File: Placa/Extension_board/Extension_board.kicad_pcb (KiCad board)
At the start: 2 copper layers, 61 x 20.3 mm, 12 parts, among them J1 Conn_01x05_Male, J2 USB_B_Micro, J3 Conn_01x04_Male, U1 STEVAL-STLCS01V1

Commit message: Version 2.1 del proyecto
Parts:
- removed D3: LED, Diode_SMD:D_0805_2012Metric
- removed R2, R3: 1Ω, Resistor_SMD:R_0805_2012Metric
- removed R5: 1kΩ, Resistor_SMD:R_0805_2012Metric
- J1: value Conn_01x05_Male -> USB_B_Micro; footprint Connector_PinHeader_1.27mm:PinHeader_1x05_P1.27mm_Vertical -> Connector_USB:USB_Micro-B_Wuerth_629105150521
- J3: footprint Connector_PinHeader_1.27mm:PinHeader_1x04_P1.27mm_Vertical -> Connector_PinHeader_1.00mm:PinHeader_1x04_P1.00mm_Vertical_SMD_Pin1Left
- R1: value 1Ω -> 1,2Ω
- moved J2 64.4 mm to (102.9, 64.8), turned to 270 degrees
- moved R1 46.6 mm to (111.8, 55.5), turned to 270 degrees
- moved R4 41.6 mm to (108.0, 55.9), turned to 270 degrees
- moved D2 35.6 mm to (108.0, 52.1), turned to 270 degrees
- moved D1 32.1 mm to (111.6, 52.1), turned to 90 degrees
- moved J3 17.0 mm to (121.9, 66.0), turned to 90 degrees
- moved J1 12.2 mm to (102.6, 49.3), turned to 270 degrees
- moved U1 11.5 mm to (121.7, 56.6), turned to 0 degrees
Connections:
- J1 pad 1: Net-(J1-Pad1) -> /SWDIO
- J1 pad 3: /GND -> /RESET
- J1 pad 4: /SWDIO -> Net-(J1-Pad4)
- J1 pad 5: /RESET -> /GND
- J3 pad 1: /V_USB -> /VIN
- R1 pad 1: Net-(R1-Pad1) -> /VIN
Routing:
- net /RXD-USB_DM: track 63.4 -> 12.2 mm, vias 2 -> 0
- net /V_USB: track 62.4 -> 11.9 mm
- net /RXD-USB_DP: track 51.4 -> 12.5 mm
- net /SWDCLK: track 64.1 -> 26.9 mm, vias 2 -> 0
- net /GND: track 104.8 -> 97.9 mm, vias 2 -> 0
- net /I2C_SDA: track 14.6 -> 10.5 mm
- net Net-(D3-Pad2): track 3.55 -> 0.00 mm
- net /SWDIO: track 23.9 -> 26.7 mm
- net Net-(R1-Pad1): track 2.62 -> 0.00 mm
- net Net-(R2-Pad2): track 2.62 -> 0.00 mm
- net Net-(D2-Pad2): track 4.10 -> 1.96 mm
- net /I2C_SCL: track 16.2 -> 17.0 mm
- net /RESET: track 26.4 -> 27.2 mm
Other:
- board size 61 x 20.3 mm -> 36.8 x 27.9 mm
- net class Default: trace_width 0.25 -> 0.4
- net class Power added: clearance 0.2, trace_width 0.5, via_dia 0.8, via_drill 0.4

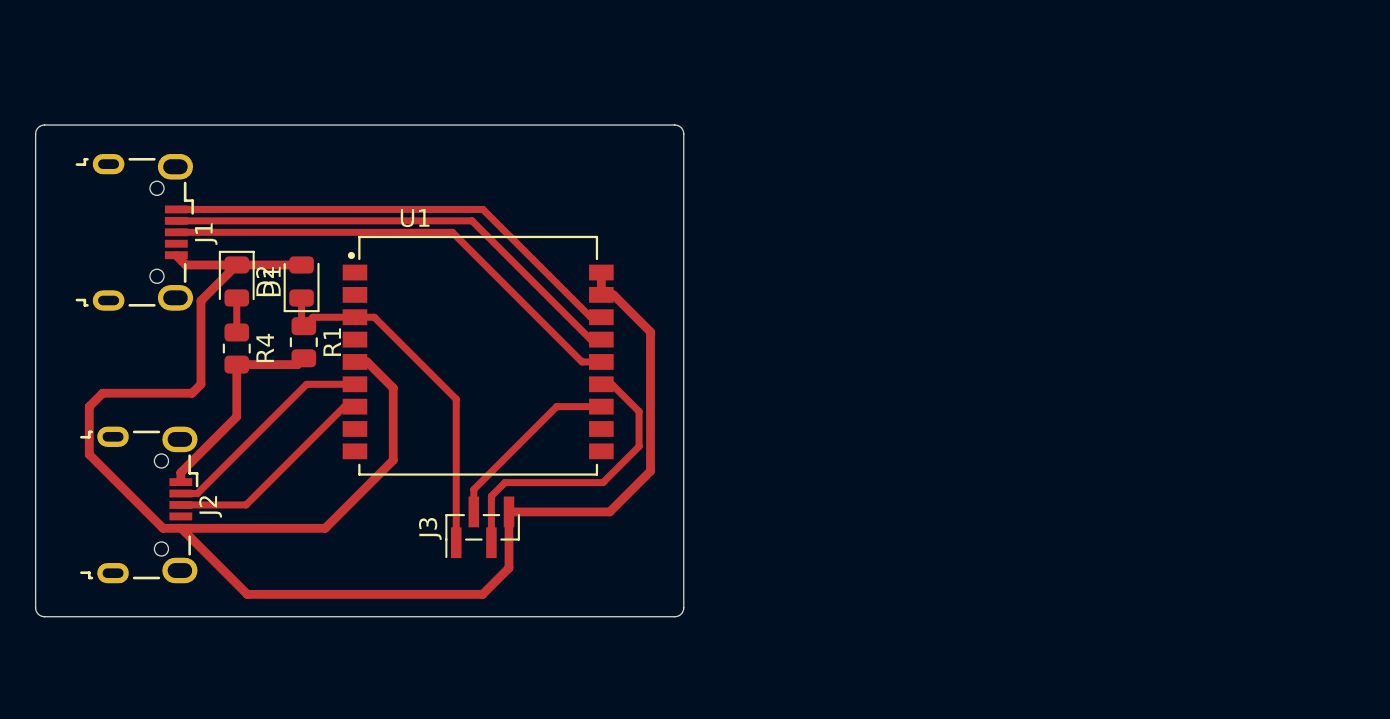
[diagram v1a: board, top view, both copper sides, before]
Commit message: Cambio de ubicacion, componentes y footprints
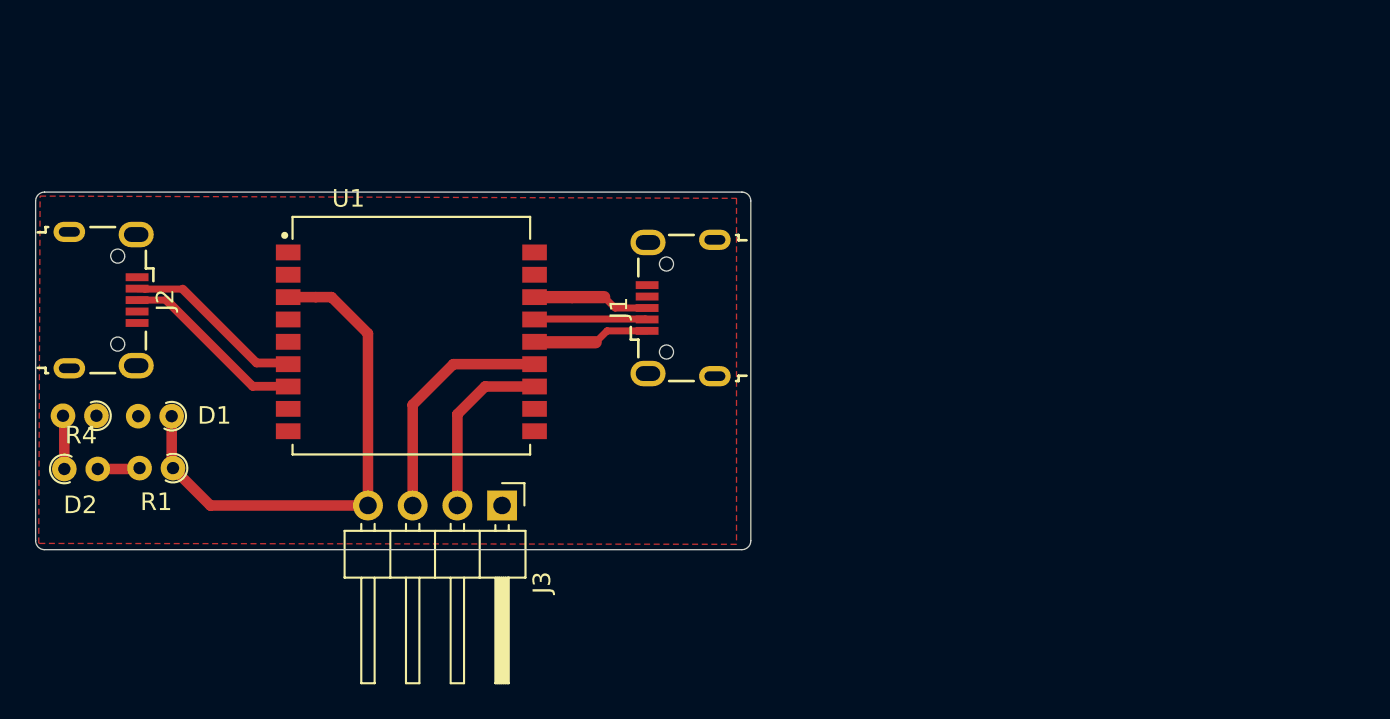
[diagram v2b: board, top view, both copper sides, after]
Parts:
- D1, D2: footprint Diode_SMD:D_0805_2012Metric -> Resistor_THT:R_Axial_DIN0204_L3.6mm_D1.6mm_P1.90mm_Vertical
- J3: footprint Connector_PinHeader_1.00mm:PinHeader_1x04_P1.00mm_Vertical_SMD_Pin1Left -> Connector_PinHeader_2.54mm:PinHeader_1x04_P2.54mm_Horizontal
- R1, R4: footprint Resistor_SMD:R_0805_2012Metric -> Resistor_THT:R_Axial_DIN0204_L3.6mm_D1.6mm_P1.90mm_Vertical
- moved J1 30.9 mm to (133.2, 53.6), turned to 90 degrees
- moved R4 12.0 mm to (98.2, 62.7), turned to 0 degrees
- moved J2 11.9 mm to (100.4, 53.1)
- moved D2 11.0 mm to (100.0, 59.7), turned to 180 degrees
- moved D1 10.6 mm to (104.2, 59.7), turned to 180 degrees
- moved R1 10.3 mm to (104.3, 62.7), turned to 180 degrees
- moved U1 3.96 mm to (117.9, 55.5)
- moved J3 1.66 mm to (123.0, 64.8), turned to 270 degrees
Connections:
- J1 pad 1: /SWDIO -> /RESET
- J1 pad 3: /RESET -> /SWDIO
- J3 pad 1: /VIN -> /GND
- J3 pad 4: /GND -> /VIN
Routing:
- net /GND: track 97.9 -> 0.00 mm
- net /RESET: track 27.2 -> 6.68 mm
- net /SWDCLK: track 26.9 -> 6.42 mm
- net /SWDIO: track 26.7 -> 6.65 mm
- net /V_USB: track 11.9 -> 2.40 mm
- net /VIN: track 20.6 -> 30.1 mm
- net /I2C_SCL: track 17.0 -> 13.6 mm
- net /RXD-USB_DP: track 12.5 -> 10.4 mm
- net /RXD-USB_DM: track 12.2 -> 10.6 mm
- net Net-(D2-Pad2): track 1.96 -> 3.06 mm
- added copper zone on F.Cu, net /GND
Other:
- board size 36.8 x 27.9 mm -> 40.6 x 20.3 mm
